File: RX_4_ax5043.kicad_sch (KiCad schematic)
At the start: 19 parts, among them J5 2118714-2, P4 CONUFL001-SMD-T, Q6 DMP2037U, U19 AX5043

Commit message: Work on cleaning up all values for things
Signed-off-by: Corey Minyard <corey@minyard.net>
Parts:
- C68, C69: value 15p -> 15p 1%
- L11, L12: value 78n -> 78n 2% Q=28
- L13: value 1n -> 1n Q=77; footprint Inductor_SMD:L_0603_1608Metric_Pad1.05x0.95mm_HandSolder -> Inductor_SMD:L_0402_1005Metric_Pad0.77x0.64mm_HandSolder
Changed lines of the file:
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@@
 			)
 		)
-		(property "Value" "78n"
+		(property "Value" "78n 2% Q=28"
 			(at 154.94 142.24 90)
 			(effects
@@
 			)
 		)
-		(property "Value" "78n"
+		(property "Value" "78n 2% Q=28"
 			(at 132.08 128.27 90)
 			(effects
@@
 			)
 		)
-		(property "Value" "15p"
+		(property "Value" "15p 1%"
 			(at 144.78 146.05 90)
 			(effects
@@
 			)
 		)
-		(property "Value" "15p"
+		(property "Value" "15p 1%"
 			(at 137.16 133.35 90)
 			(effects
@@
 			)
 		)
-		(property "Value" "1n"
+		(property "Value" "1n Q=77"
 			(at 165.1 142.24 90)
 			(effects
@@
 			)
 		)
-		(property "Footprint" "Inductor_SMD:L_0603_1608Metric_Pad1.05x0.95mm_HandSolder"
+		(property "Footprint" "Inductor_SMD:L_0402_1005Metric_Pad0.77x0.64mm_HandSolder"
 			(at 162.56 142.24 0)
 			(effects

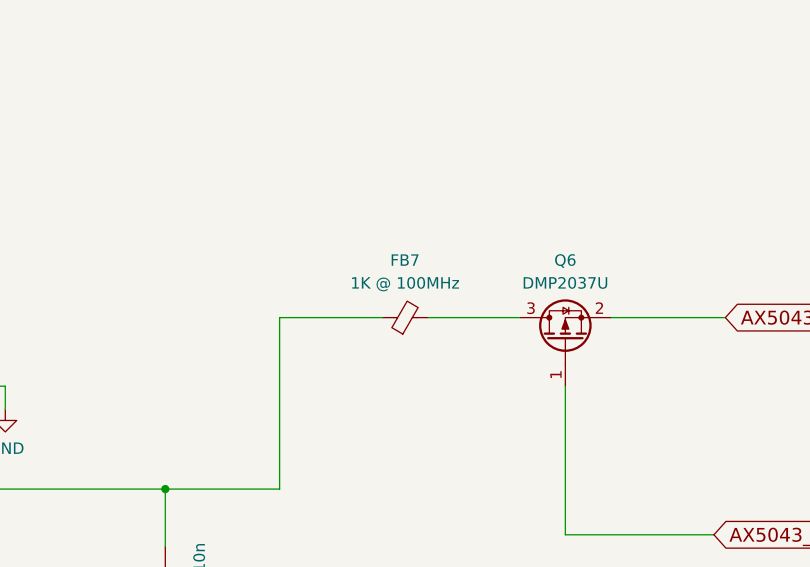
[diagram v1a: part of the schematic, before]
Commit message: More work on components
Signed-off-by: Corey Minyard <corey@minyard.net>
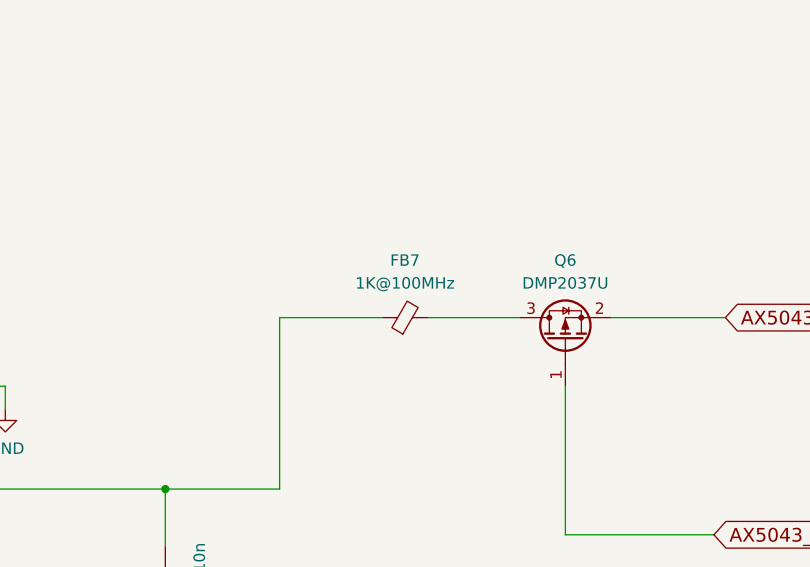
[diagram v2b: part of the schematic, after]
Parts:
- FB7: value 1K @ 100MHz -> 1K@100MHz
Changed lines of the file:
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@@
 			)
 		)
-		(property "Value" "1K @ 100MHz"
+		(property "Value" "1K@100MHz"
 			(at 267.9319 68.58 90)
 			(effects

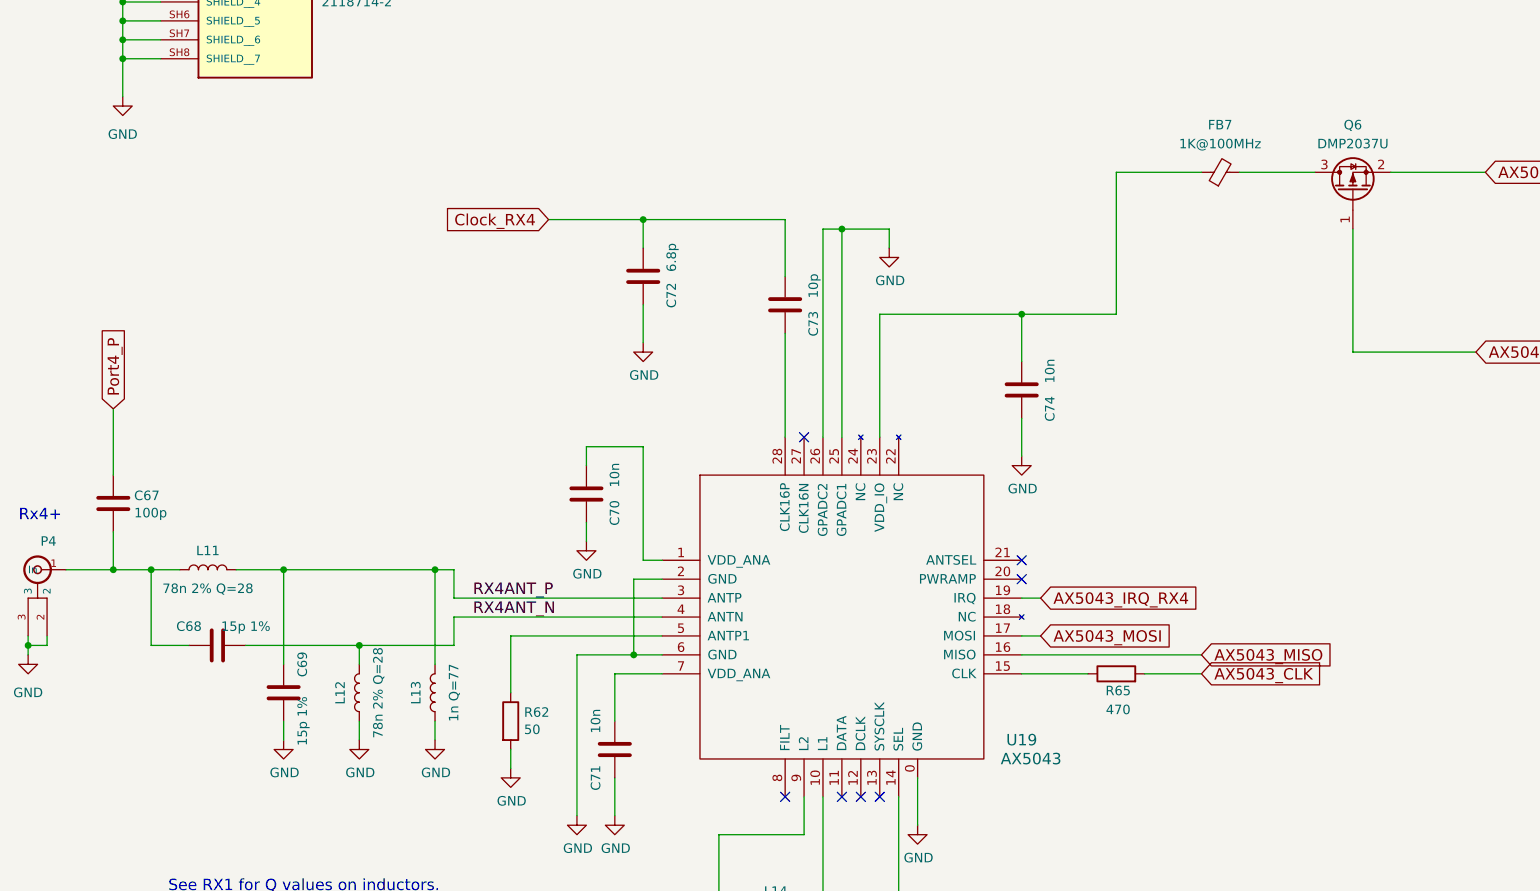
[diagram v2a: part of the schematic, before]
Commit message: Lots of updates to ease manufacturing
Component changes, changes in the formatting of the values, etc.

Signed-off-by: Corey Minyard <corey@minyard.net>
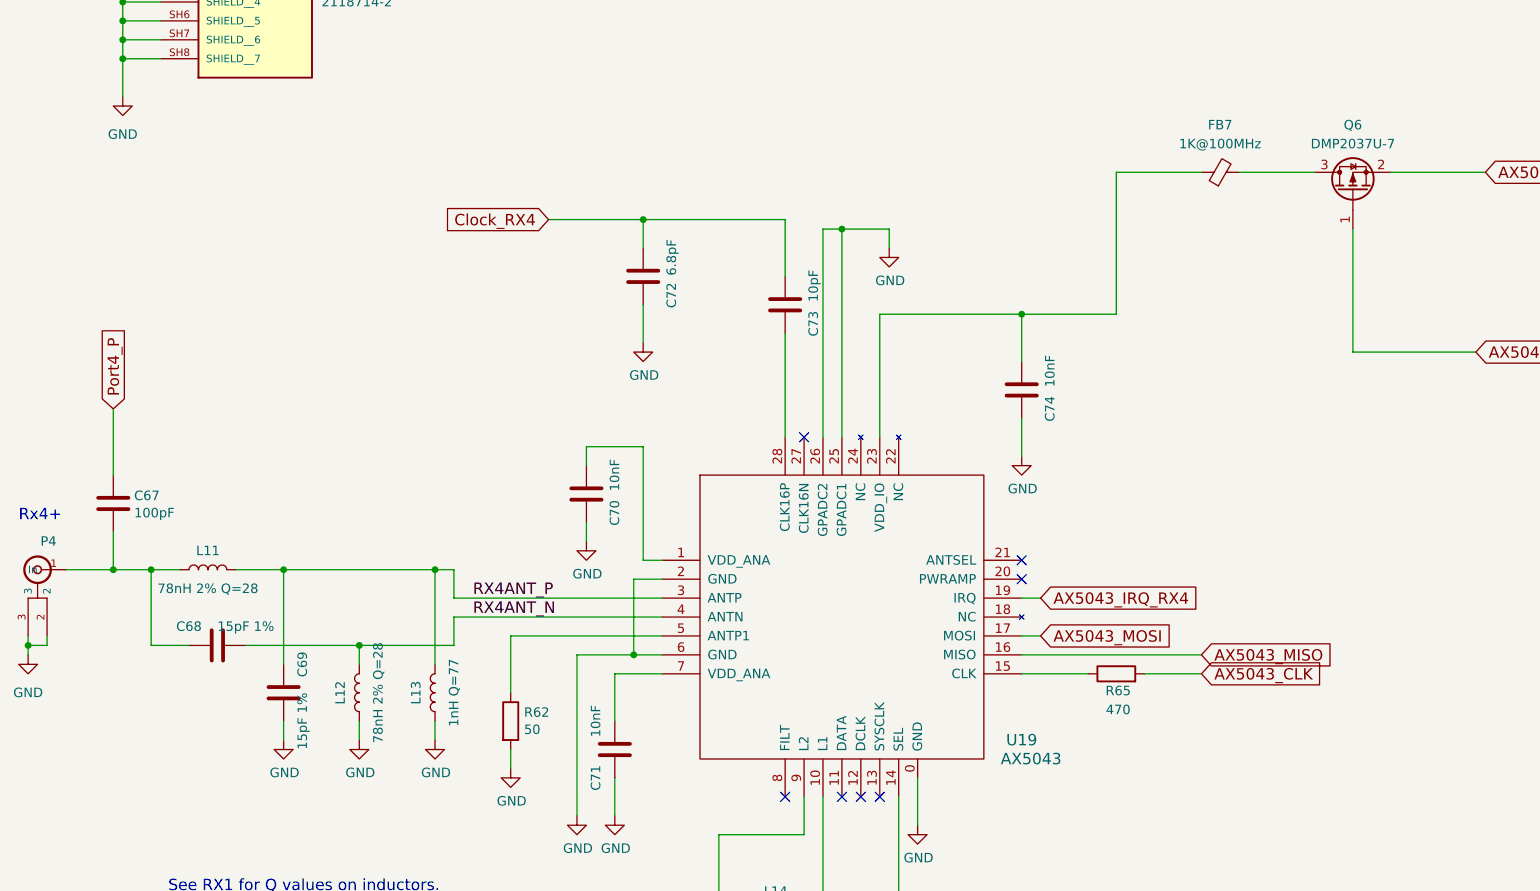
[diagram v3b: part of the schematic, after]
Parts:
- C67: value 100p -> 100pF
- C68, C69: value 15p 1% -> 15pF 1%
- C70, C71, C74: value 10n -> 10nF
- C72: value 6.8p -> 6.8pF
- C73: value 10p -> 10pF
- L11, L12: value 78n 2% Q=28 -> 78nH 2% Q=28
- L13: value 1n Q=77 -> 1nH Q=77
- Q6: value DMP2037U -> DMP2037U-7
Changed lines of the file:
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@@
 			)
 		)
-		(property "Value" "6.8p"
+		(property "Value" "6.8pF"
 			(at 194.31 83.82 90)
 			(effects
@@
 			)
 		)
-		(property "Value" "10p"
+		(property "Value" "10pF"
 			(at 213.36 87.63 90)
 			(effects
@@
 			)
 		)
-		(property "Value" "78n 2% Q=28"
+		(property "Value" "78nH 2% Q=28"
 			(at 154.94 142.24 90)
 			(effects
@@
 			)
 		)
-		(property "Value" "78n 2% Q=28"
+		(property "Value" "78nH 2% Q=28"
 			(at 132.08 128.27 90)
 			(effects
@@
 			)
 		)
-		(property "Value" "10n"
+		(property "Value" "10nF"
 			(at 186.69 113.03 90)
 			(effects
@@
 			)
 		)
-		(property "Value" "DMP2037U"
+		(property "Value" "DMP2037U-7"
 			(at 285.75 68.58 90)
 			(effects
@@
 			)
 		)
-		(property "Value" "15p 1%"
+		(property "Value" "15pF 1%"
 			(at 144.78 146.05 90)
 			(effects
@@
 			)
 		)
-		(property "Value" "15p 1%"
+		(property "Value" "15pF 1%"
 			(at 137.16 133.35 90)
 			(effects
@@
 			)
 		)
-		(property "Value" "10n"
+		(property "Value" "10nF"
 			(at 245.11 99.06 90)
 			(effects
@@
 			)
 		)
-		(property "Value" "1n Q=77"
+		(property "Value" "1nH Q=77"
 			(at 165.1 142.24 90)
 			(effects
@@
 			)
 		)
-		(property "Value" "100p"
+		(property "Value" "100pF"
 			(at 122.174 118.11 0)
 			(effects
@@
 			)
 		)
-		(property "Value" "10n"
+		(property "Value" "10nF"
 			(at 184.15 146.05 90)
 			(effects

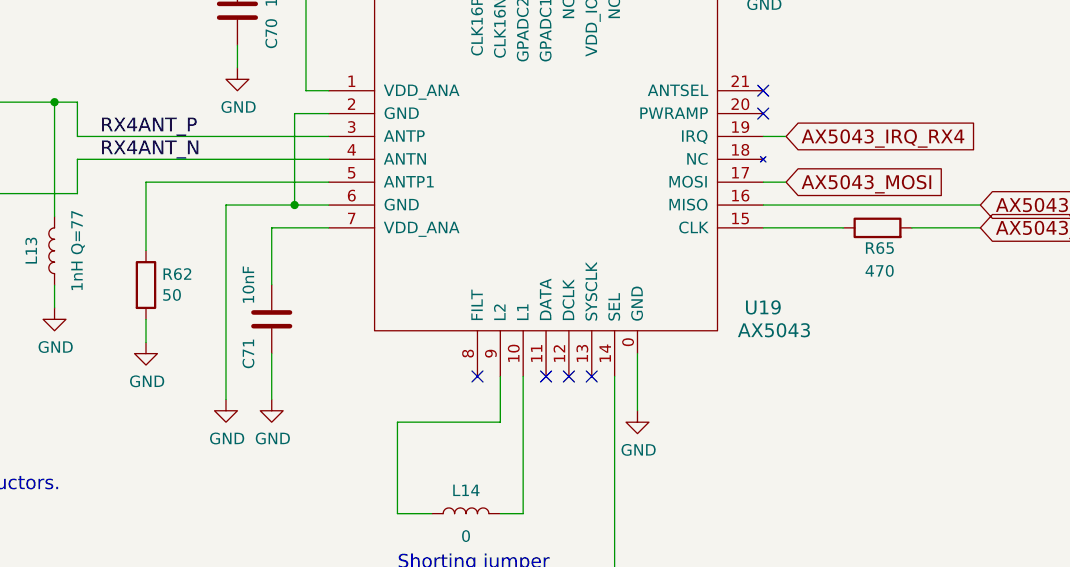
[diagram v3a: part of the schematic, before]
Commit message: Update all resistors to have an ohm symbol
Make it more clean in the BOM what they are.

Signed-off-by: Corey Minyard <corey@minyard.net>
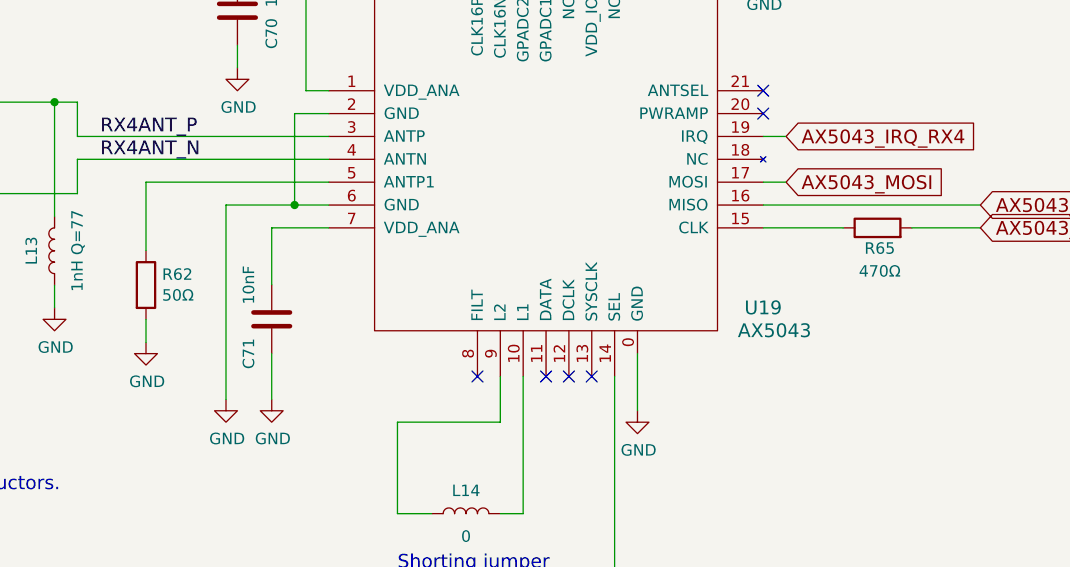
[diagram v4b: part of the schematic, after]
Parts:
- R62: value 50 -> 50Ω
- R65: value 470 -> 470Ω
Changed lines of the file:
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@@
 			)
 		)
-		(property "Value" "50"
+		(property "Value" "50Ω"
 			(at 174.498 147.193 0)
 			(effects
@@
 			)
 		)
-		(property "Value" "470"
+		(property "Value" "470Ω"
 			(at 254.254 144.526 90)
 			(effects

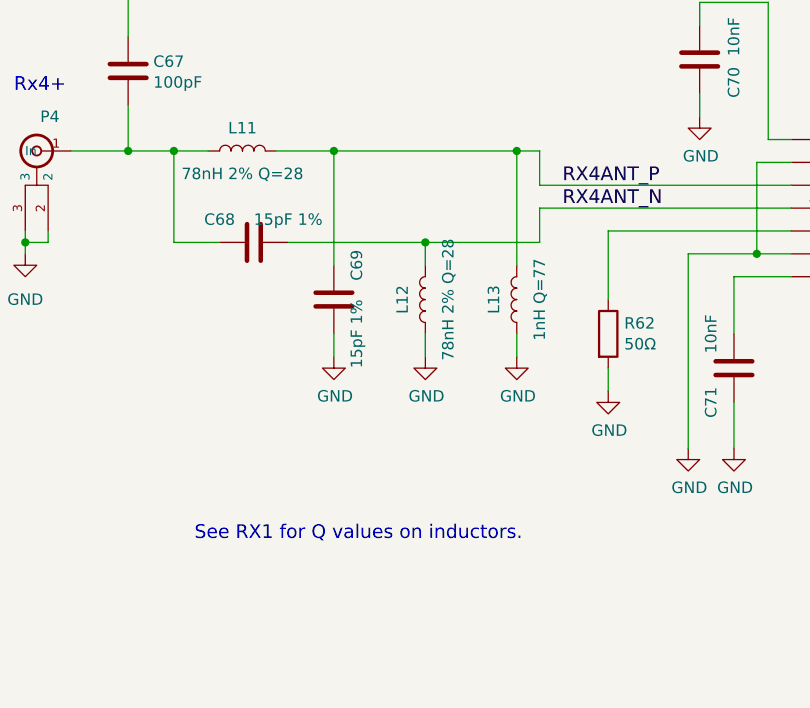
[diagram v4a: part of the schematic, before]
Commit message: Massive rework of filtering and inductors
Now that I know how inductors really work.

Signed-off-by: Corey Minyard <corey@minyard.net>
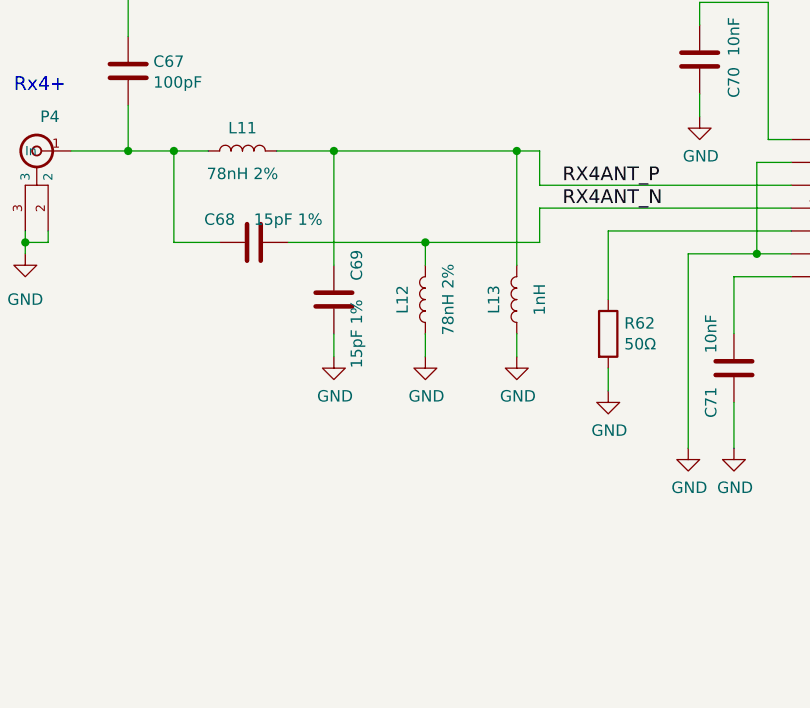
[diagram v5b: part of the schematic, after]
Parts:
- L11, L12: value 78nH 2% Q=28 -> 78nH 2%
- L13: value 1nH Q=77 -> 1nH
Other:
- note removed: "See RX1 for Q values on inductors."
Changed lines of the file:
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@@
 		)
 	)
-	(text "See RX1 for Q values on inductors."
-		(exclude_from_sim no)
-		(at 126.746 169.164 0)
-		(effects
-			(font
-				(size 1.524 1.524)
-			)
-			(justify left bottom)
-		)
-	)
 	(junction
 		(at 152.4 135.89)
@@
 			)
 		)
-		(property "Value" "78nH 2% Q=28"
+		(property "Value" "78nH 2%"
 			(at 154.94 142.24 90)
 			(effects
@@
 			)
 		)
-		(property "Value" "78nH 2% Q=28"
+		(property "Value" "78nH 2%"
 			(at 132.08 128.27 90)
 			(effects
@@
 			)
 		)
-		(property "Value" "1nH Q=77"
+		(property "Value" "1nH"
 			(at 165.1 142.24 90)
 			(effects

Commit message: Have the BOM file fixer output xls, not csv
The omega symbol gets translated properly from xls.

Signed-off-by: Corey Minyard <corey@minyard.net>
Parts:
- FB7: footprint Resistor_SMD:R_0603_1608Metric_Pad0.98x0.95mm_HandSolder -> Inductor_SMD:L_0603_1608Metric_Pad1.05x0.95mm_HandSolder
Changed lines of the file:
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@@
 			)
 		)
-		(property "Footprint" "Resistor_SMD:R_0603_1608Metric_Pad0.98x0.95mm_HandSolder"
+		(property "Footprint" "Inductor_SMD:L_0603_1608Metric_Pad1.05x0.95mm_HandSolder"
 			(at 267.97 74.168 90)
 			(effects

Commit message: Minor fixes for BOM values
Signed-off-by: Corey Minyard <corey@minyard.net>
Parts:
- FB7: value 1K@100MHz -> 1KΩ@100MHz
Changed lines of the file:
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@@
 			)
 		)
-		(property "Value" "1K@100MHz"
+		(property "Value" "1KΩ@100MHz"
 			(at 267.9319 68.58 90)
 			(effects

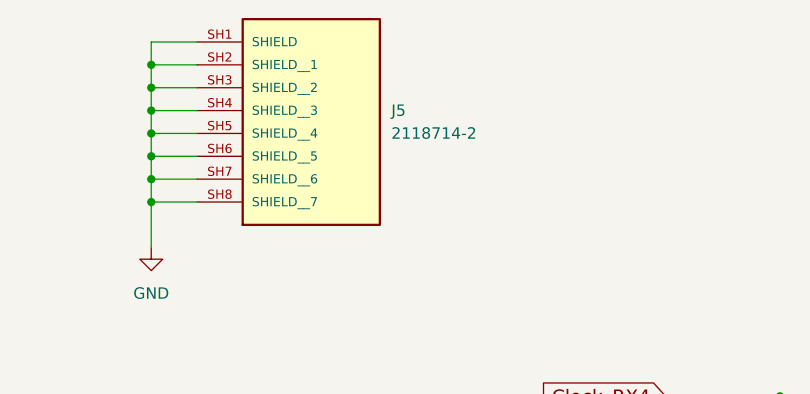
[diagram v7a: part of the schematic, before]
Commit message: Renumber shields and PC104 sockets
Separate out shields into their own designator category.

Make the PC104 sockets J1 and J2 to make it easier to move to other
boards.

Signed-off-by: Corey Minyard <corey@minyard.net>
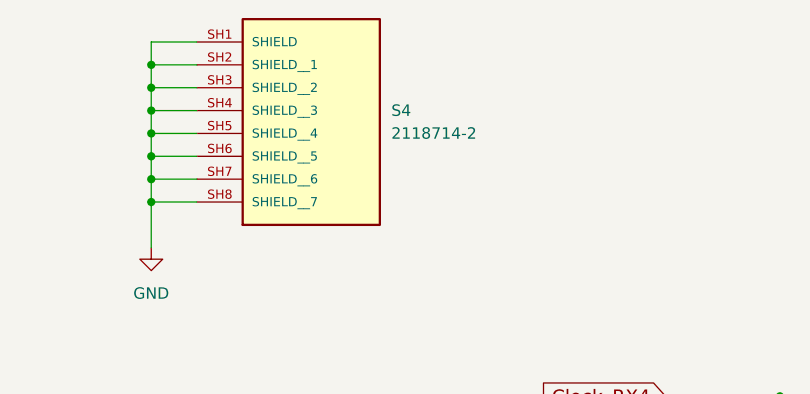
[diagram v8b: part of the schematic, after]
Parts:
- renumbered J5 to S4
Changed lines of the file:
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@@
 		(dnp no)
 		(fields_autoplaced yes)
-		(property "Reference" "J5"
+		(property "Reference" "S4"
 			(at 147.32 46.9899 0)
 			(effects
@@
 			(project "PacSat_AFSK"
 				(path "/cc9f42d2-6985-41ac-acab-5ab7b01c5b38/d9a83ee4-3280-49b9-88b8-54d26cbd8ed1/7fb6f4ad-3f2f-474c-8e36-07b875720381"
-					(reference "J5")
+					(reference "S4")
 					(unit 1)
 				)
